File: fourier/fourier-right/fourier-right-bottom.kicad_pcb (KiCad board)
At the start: 2 copper layers, 141.4 x 92.2 mm, 8 parts

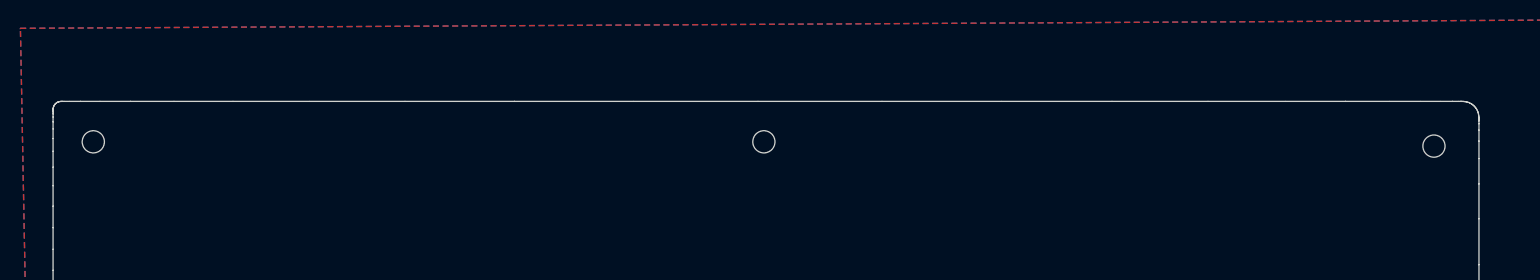
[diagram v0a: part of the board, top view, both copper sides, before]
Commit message: Top height and center hole adjusment
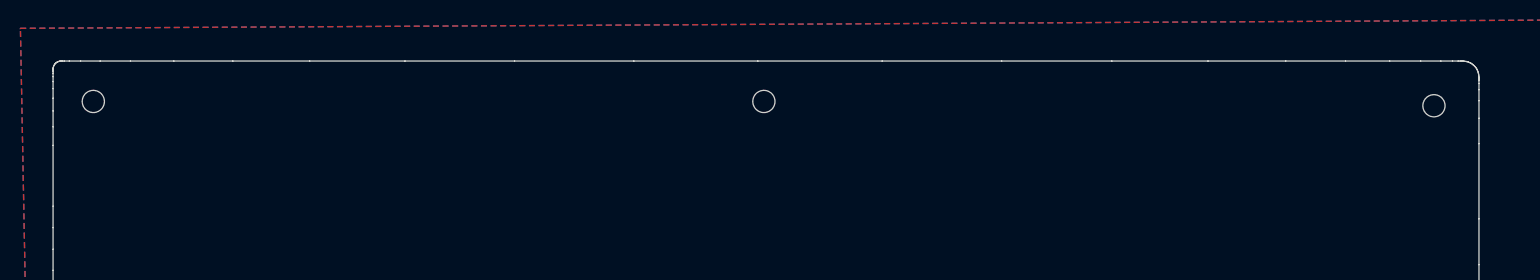
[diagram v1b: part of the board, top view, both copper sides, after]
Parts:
- removed G***: LOGO, Keebio-Art:Keebio-TwoTone
- moved REF** 4.00 mm to (156.4, 33.5)
- moved REF** 4.00 mm to (90.0, 33.1)
- moved REF** 4.00 mm to (23.6, 33.1)
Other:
- board size 141.4 x 92.2 mm -> 141.4 x 96.2 mm

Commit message: rotate right top to correct orientation and upgraded to KiCad 5.99
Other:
- net class Default removed
